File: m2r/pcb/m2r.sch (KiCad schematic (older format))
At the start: 116 parts, among them IC1 ADP3338, IC10 STM32F303C, IC11 ADP3333, IC2 ADP3335, IC3 ADuM1201, IC4 ADuM1201, IC5 ADuM1201, IC6 MTX2, IC7 ADL5324, IC8 MAX-7Q, IC9 ALM-2712, P1 CONN_2, P2 CONN_2, P3 CONN_4, P4 CONN_4, P5 CONN_4, P6 SWD, P7 SMA, P8 CONN_2, X1 BAT BOX, X10 8M, X2 ARM SW, X3 HOUSING, X4 HOUSING, X5 HOUSING, X6 HOUSING, X7 HOUSING, X8 RG LED, X9 HOUSING

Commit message: a good looking ratsnest
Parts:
- ANT1: footprint (none) -> m2r:JDGA_QUAD_V
- C1, C10, C11, C12, C13, C14, C15, C17, C2, C23, C24, C25, C26, C27, C28, C29, C3, C30, C31, C32, C33, C34, C35, C36, C4, C5, C6, C7, C8, C9: footprint Capacitors_SMD:c_0603 -> m2r:C0603
- C16, C19, C20, C21, C22: footprint Capacitors_SMD:c_0402 -> m2r:C0402
- C18: footprint Capacitors_SMD:c_1206 -> m2r:C1206
- D1, D2, D3, D4, D5, D6: footprint Capacitors_SMD:c_0603 -> m2r:LED0603
- GS1, GS2: footprint Connect:GS3 -> m2r:SJ3
- IC1: footprint SMD_Packages:SOT223 -> m2r:SOT223
- IC10: footprint Housings_QFP:lqfp-48 -> m2r:LQFP48
- IC11: footprint (none) -> m2r:MSOP8
- IC2: footprint Housings_SSOP:MSOP-8 -> m2r:MSOP8
- IC3, IC4, IC5: footprint Housings_SOIC:SOIC-8_N -> m2r:SOIC8
- IC6: footprint (none) -> m2r:MTX2
- IC7: footprint Housings_SOT-89:SOT89-3_Housing -> m2r:SOT89-3
- IC8: footprint (none) -> m2r:MAX-7Q
- IC9: footprint (none) -> m2r:ALM-2712
- L1, L2: footprint SMD_Packages:SM0603 -> m2r:L0603
- L3: footprint SMD_Packages:SM0402 -> m2r:L0402
- P1, P2, P8: footprint JST_PA:S02B-PASK-2 -> m2r:S02B-PASK-2
- P3, P4, P5: footprint JST_PA:S04B-PASK-2 -> m2r:S04B-PASK-2
- P6: footprint (none) -> m2r:FTSH-105-01-F-D-K
- P7: footprint (none) -> m2r:SMA-142-0701-801
- R1, R10, R11, R12, R13, R14, R2, R4, R5, R6, R7, R8, R9: footprint SMD_Packages:SM0603_Resistor -> m2r:R0603
- R3: footprint SMD_Packages:SM0402_r -> m2r:R0402
- TP1, TP10, TP11, TP12, TP13, TP14, TP15, TP16, TP17, TP18, TP19, TP2, TP20, TP21, TP22, TP23, TP24, TP25, TP3, TP4, TP5, TP6, TP7, TP8, TP9: footprint Measurement_Points:Measurement_Point_Round-SMD-Pad_Small -> m2r:TESTPAD
- X10: footprint Crystals:Crystal_HC49-U_Vertical -> m2r:HC49S
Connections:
- net +BATT: now also P2.1 (P1); no longer P2.2 (PM)
- net BAT_MON: now also IC10.16 (PA6); no longer IC10.10 (PA0_WKUP)
- net GND: now also P1.2 (PM); no longer P1.1 (P1)
- net LED_1: now also IC10.25 (PB12); no longer IC10.14 (PA4)
- net LED_2: now also IC10.26 (PB13); no longer IC10.15 (PA5)
- net LED_3: now also IC10.27 (PB14); no longer IC10.16 (PA6)
- net LED_4: now also IC10.28 (PB15); no longer IC10.17 (PA7)
- net LED_A: now also IC10.14 (PA4); no longer IC10.27 (PB14)
- net LED_C: now also IC10.15 (PA5); no longer IC10.28 (PB15)
- net NTX2B_P0: now also IC10.19 (PB1); no longer IC10.26 (PB13)
- net NTX2B_P1: now also IC10.20 (PB2); no longer IC10.25 (PB12)
- net RB_RX: now also IC10.30 (PA9); no longer IC10.12 (PA2)
- net RB_TX: now also IC10.31 (PA10); no longer IC10.13 (PA3)
- net SER_IN: now also IC10.13 (PA3); no longer IC10.31 (PA10)
- net SER_OUT: now also IC10.12 (PA2); no longer IC10.30 (PA9)
- new net: P1.1 (P1), P2.2 (PM)
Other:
- moved on the sheet: TP13, TP14, TP15, TP16, TP17, TP24, TP25

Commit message: further pcb work i guess
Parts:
- added D10, D11, D7, D8, D9: ESD5V3S1U, m2r:TSLP-2-17, symbol ESD5V3S1U
- added X11, X12, X13, X14: M3 MOUNT, m2r:M3_MOUNT, symbol PART
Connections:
- net +5V: now also D7.1 (C)
- net +BATT: now also P2.2 (PM), D8.1 (C); no longer P2.1 (P1)
- net GND: now also P1.1 (P1), D10.2 (A), D11.2 (A), D7.2 (A), D8.2 (A), D9.2 (A); no longer P1.2 (PM)
- net LED_A: now also IC10.15 (PA5); no longer IC10.14 (PA4)
- net LED_C: now also IC10.14 (PA4), D10.1 (C); no longer IC10.15 (PA5)
- net at GS2.2 (G2), P7.1 (RF): now also D9.1 (C)
- net at P8.1 (P1), R4.1, R5.1: now also D11.1 (C)
- new net: P1.2 (PM), P2.1 (P1)
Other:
- moved on the sheet: P7, P8, X8, X9

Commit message: 2 airwires to go
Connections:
- net +5V: now also R9.1; no longer R9.2
- net LED_A: now also IC10.14 (PA4); no longer IC10.15 (PA5)
- net LED_C: now also IC10.15 (PA5), P8.1 (P1); no longer IC10.14 (PA4), P8.2 (PM)
- net at D11.1 (C), R4.1, R5.1: now also P8.2 (PM); no longer P8.1 (P1)
- net at R7.2: now also R9.2; no longer R9.1
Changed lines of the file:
@@
 F 4 "1830747" H 10500 3900 60  0001 C CNN "Farnell"
 	1    10500 3900
-	1    0    0    -1
+	1    0    0    1
 $EndComp
 $Comp
@@
 F 4 "2331989" H 10150 4650 60  0001 C CNN "Farnell"
 	1    10150 4650
-	0    1    1    0
+	0    -1   1    0
 $EndComp
 $Comp
@@
 Text GLabel 3350 6000 2    60   Output ~ 0
 LED_4
+Text GLabel 3350 3250 2    60   Output ~ 0
+LED_A
 Text GLabel 3350 3350 2    60   Output ~ 0
-LED_A
-Text GLabel 3350 3250 2    60   Output ~ 0
 LED_C
 $Comp

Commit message: pretty silk
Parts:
- C22: value 6.2p -> 6p2
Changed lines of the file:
@@
 P 9150 2950
 F 0 "C22" H 9150 3050 40  0000 L CNN
-F 1 "6.2p" H 9156 2865 40  0000 L CNN
+F 1 "6p2" H 9156 2865 40  0000 L CNN
 F 2 "m2r:C0402" H 9188 2800 30  0001 C CNN
 F 3 "" H 9150 2950 60  0000 C CNN

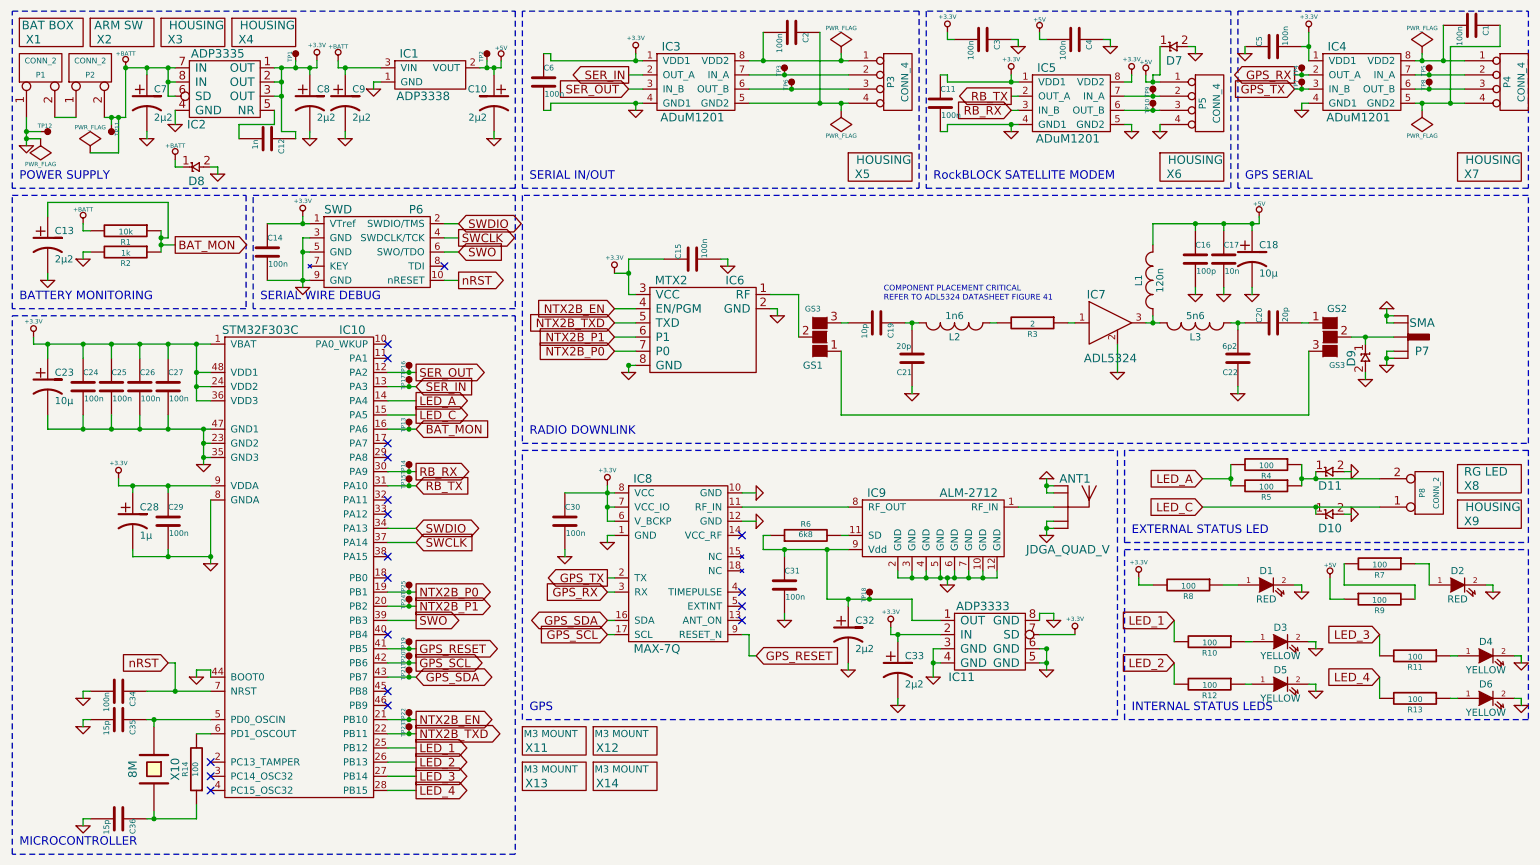
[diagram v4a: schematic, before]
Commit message: changed ESD diode to 12V one
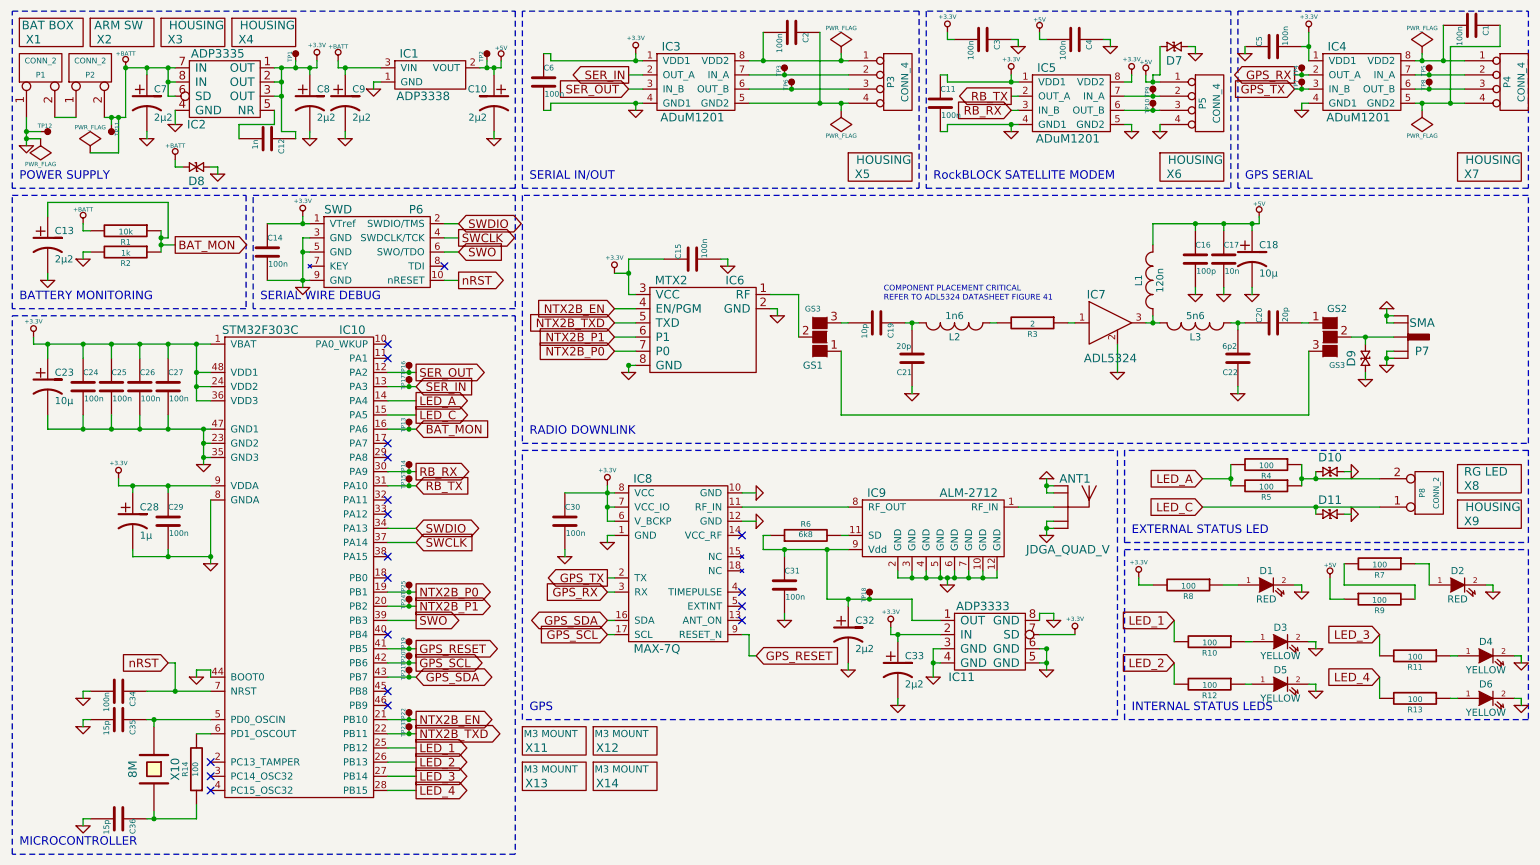
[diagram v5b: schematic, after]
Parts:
- removed D10, D11, D7, D8, D9: ESD5V3S1U, m2r:TSLP-2-17, symbol ESD5V3S1U
- added D10, D11, D7, D8, D9: CGA0402MLC-12G, m2r:R0402, symbol CGA0402MLC-12G
- IC11: Farnell (none) -> 2376929
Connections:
- net +5V: now also D7.1
- net +BATT: now also D8.1
- net GND: now also D10.1, D11.1, D7.2, D8.2, D9.2
- net LED_C: now also D11.2
- net at GS2.2 (G2), P7.1 (RF): now also D9.1
- net at P8.2 (PM), R4.1, R5.1: now also D10.2
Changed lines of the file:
@@
 LIBS:mocd207m
 LIBS:esd5v3s1u
+LIBS:cga0402mlc-12g
 LIBS:m2r-cache
 EELAYER 24 0
@@
 F 2 "m2r:MSOP8" H 7050 4800 60  0001 C CNN
 F 3 "" H 7050 4800 60  0000 C CNN
+F 4 "2376929" H 7050 4800 60  0001 C CNN "Farnell"
 	1    7050 4800
 	1    0    0    -1
@@
 $EndComp
 $Comp
-L ESD5V3S1U D10
-U 1 1 53D09D94
-P 9700 4050
-F 0 "D10" H 9800 3950 60  0000 C CNN
-F 1 "ESD5V3S1U" H 9790 4140 60  0001 C CNN
-F 2 "m2r:TSLP-2-17" H 9700 4050 60  0001 C CNN
-F 3 "" H 9700 4050 60  0000 C CNN
-F 4 "2212811" H 9700 4050 60  0001 C CNN "Farnell"
-	1    9700 4050
+L CGA0402MLC-12G D8
+U 1 1 53D01898
+P 1700 1600
+F 0 "D8" H 1800 1500 60  0000 C CNN
+F 1 "CGA0402MLC-12G" H 1800 1710 60  0001 C CNN
+F 2 "m2r:R0402" H 1700 1600 10  0001 C CNN
+F 3 "" H 1700 1600 60  0000 C CNN
+F 4 "2368169" H 1700 1600 60  0001 C CNN "Farnell"
+	1    1700 1600
 	1    0    0    -1
 $EndComp
 $Comp
-L ESD5V3S1U D11
-U 1 1 53CEBD54
-P 9700 3750
-F 0 "D11" H 9800 3650 60  0000 C CNN
-F 1 "ESD5V3S1U" H 9790 3840 60  0001 C CNN
-F 2 "m2r:TSLP-2-17" H 9700 3750 60  0001 C CNN
-F 3 "" H 9700 3750 60  0000 C CNN
-F 4 "2212811" H 9700 3750 60  0001 C CNN "Farnell"
-	1    9700 3750
+L CGA0402MLC-12G D7
+U 1 1 53D0258B
+P 8600 750
+F 0 "D7" H 8700 650 60  0000 C CNN
+F 1 "CGA0402MLC-12G" H 8700 860 60  0001 C CNN
+F 2 "m2r:R0402" H 8600 750 10  0001 C CNN
+F 3 "" H 8600 750 60  0000 C CNN
+F 4 "2368169" H 8600 750 60  0001 C CNN "Farnell"
+	1    8600 750
 	1    0    0    -1
 $EndComp
 $Comp
-L ESD5V3S1U D9
-U 1 1 53CEBDEC
+L CGA0402MLC-12G D9
+U 1 1 53D02CEB
 P 10050 2850
 F 0 "D9" H 10150 2750 60  0000 C CNN
-F 1 "ESD5V3S1U" H 10140 2940 60  0001 C CNN
-F 2 "m2r:TSLP-2-17" H 10050 2850 60  0001 C CNN
+F 1 "CGA0402MLC-12G" H 10150 2960 60  0001 C CNN
+F 2 "m2r:R0402" H 10050 2850 10  0001 C CNN
 F 3 "" H 10050 2850 60  0000 C CNN
-F 4 "2212811" H 10050 2850 60  0001 C CNN "Farnell"
+F 4 "2368169" H 10050 2850 60  0001 C CNN "Farnell"
 	1    10050 2850
 	0    1    1    0
 $EndComp
 $Comp
-L ESD5V3S1U D7
-U 1 1 53CEC0C9
-P 8600 750
-F 0 "D7" H 8700 650 60  0000 C CNN
-F 1 "ESD5V3S1U" H 8690 840 60  0001 C CNN
-F 2 "m2r:TSLP-2-17" H 8600 750 60  0001 C CNN
-F 3 "" H 8600 750 60  0000 C CNN
-F 4 "2212811" H 8600 750 60  0001 C CNN "Farnell"
-	1    8600 750
-	1    0    0    -1
+L CGA0402MLC-12G D10
+U 1 1 53D031DA
+P 9900 3750
+F 0 "D10" H 10000 3650 60  0000 C CNN
+F 1 "CGA0402MLC-12G" H 10000 3860 60  0001 C CNN
+F 2 "m2r:R0402" H 9900 3750 10  0001 C CNN
+F 3 "" H 9900 3750 60  0000 C CNN
+F 4 "2368169" H 9900 3750 60  0001 C CNN "Farnell"
+	1    9900 3750
+	-1   0    0    1
 $EndComp
 $Comp
-L ESD5V3S1U D8
-U 1 1 53CEC6CF
-P 1700 1600
-F 0 "D8" H 1800 1500 60  0000 C CNN
-F 1 "ESD5V3S1U" H 1790 1690 60  0001 C CNN
-F 2 "m2r:TSLP-2-17" H 1700 1600 60  0001 C CNN
-F 3 "" H 1700 1600 60  0000 C CNN
-F 4 "2212811" H 1700 1600 60  0001 C CNN "Farnell"
-	1    1700 1600
-	1    0    0    -1
+L CGA0402MLC-12G D11
+U 1 1 53D036C9
+P 9900 4050
+F 0 "D11" H 10000 3950 60  0000 C CNN
+F 1 "CGA0402MLC-12G" H 10000 4160 60  0001 C CNN
+F 2 "m2r:R0402" H 9900 4050 10  0001 C CNN
+F 3 "" H 9900 4050 60  0000 C CNN
+F 4 "2368169" H 9900 4050 60  0001 C CNN "Farnell"
+	1    9900 4050
+	-1   0    0    1
 $EndComp
 $EndSCHEMATC

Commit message: spec alt part for m2r 10p capacitor
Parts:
- C19: Alt Farnell (none) -> 1327593
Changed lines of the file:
@@
 F 3 "" H 6600 2700 60  0000 C CNN
 F 4 "1885332" H 6600 2700 60  0001 C CNN "Farnell"
+F 5 "1327593" H 6600 2700 60  0001 C CNN "Alt Farnell"
 	1    6600 2700
 	0    1    1    0
